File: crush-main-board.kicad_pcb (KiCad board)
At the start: 2 copper layers, 27 parts, among them J1 USB_B_Micro, J10 4x4_Header, J11 3x4_Header, J12 3x4_Header, J13 6x2_Header, J14 3x1_Header, J2 3x3 Header, J3 3x3 Header, J4 3x3 Header, J5 3x2 Header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

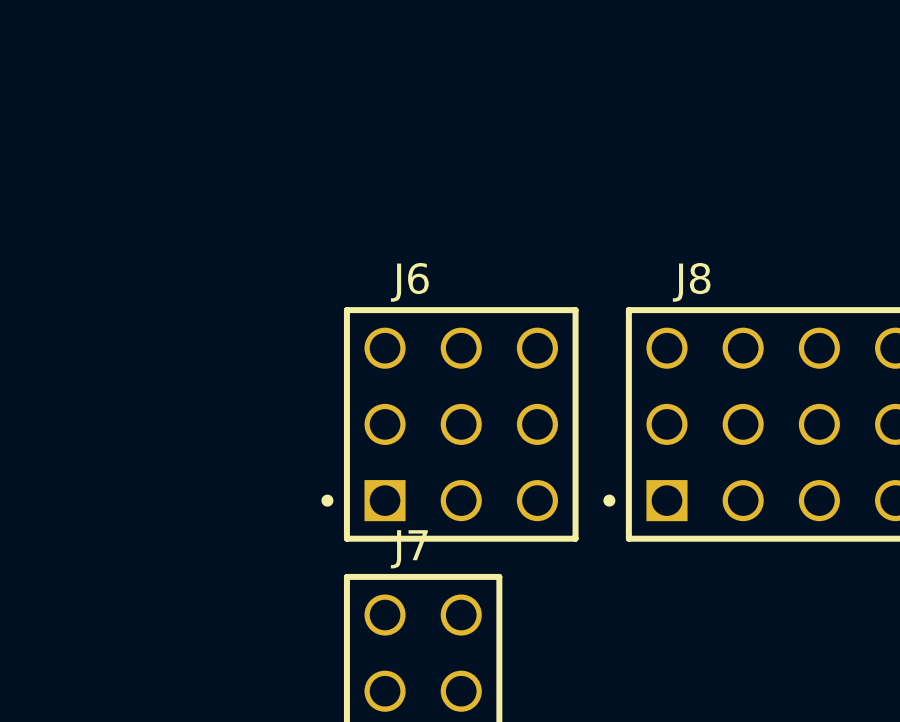
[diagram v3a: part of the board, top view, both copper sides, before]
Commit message: Fixed SPI header and updated footprint accordingly
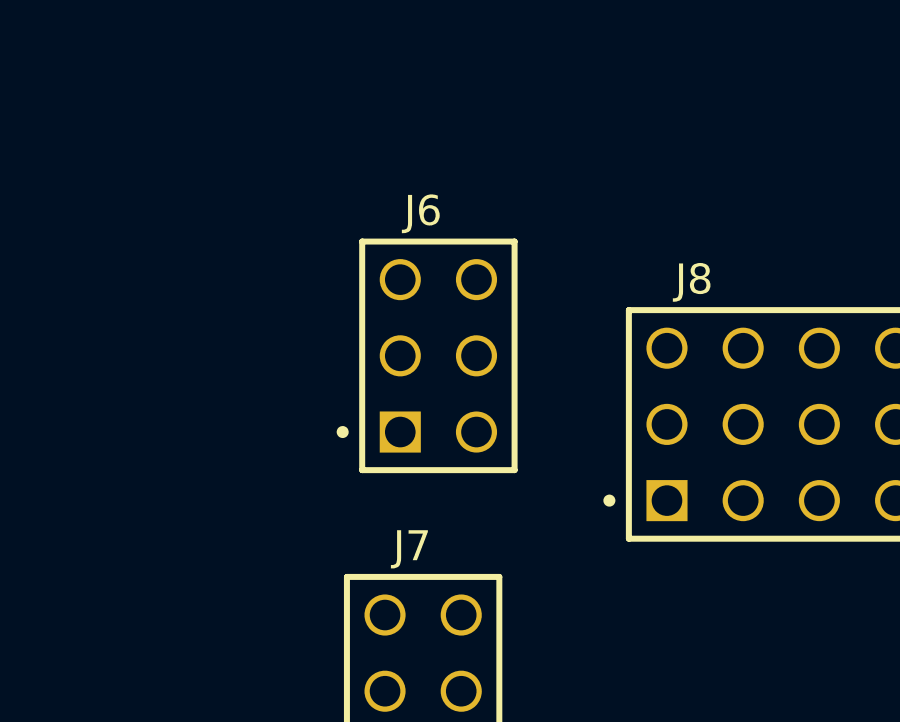
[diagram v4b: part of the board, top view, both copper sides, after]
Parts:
- J6: value 3x3 Header -> 3x2 Header; footprint Crush_Mainboard_Footprints:3x3_Header -> Crush_Mainboard_Footprints:3x2_Header
- moved J6 2.41 mm to (113.0, 104.1)
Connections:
- J13 pad 06: SPI_CS -> DIO30
- J6 pad 01: DIO30 -> DIO31
- J6 pad 04: DIO31 -> DIO32

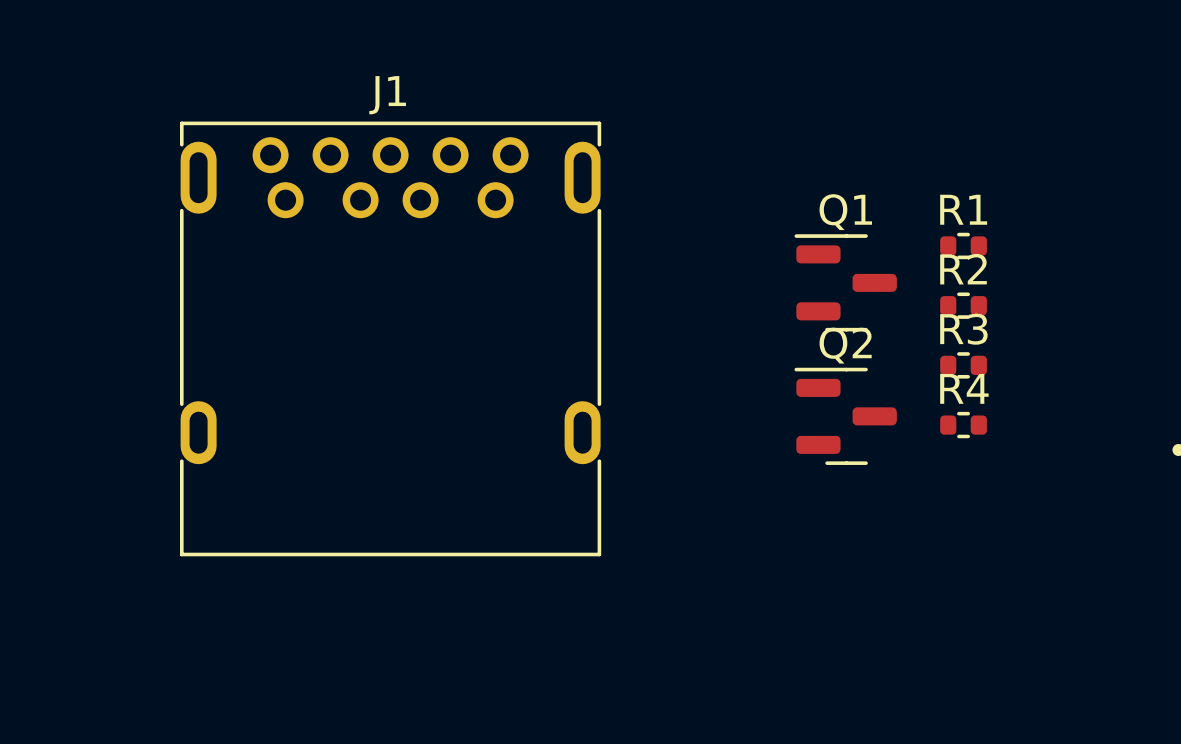
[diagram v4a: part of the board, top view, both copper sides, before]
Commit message: Added thruster battery monitoring circuit
There is no footprint assigned for an I2C isolator and resistors yet
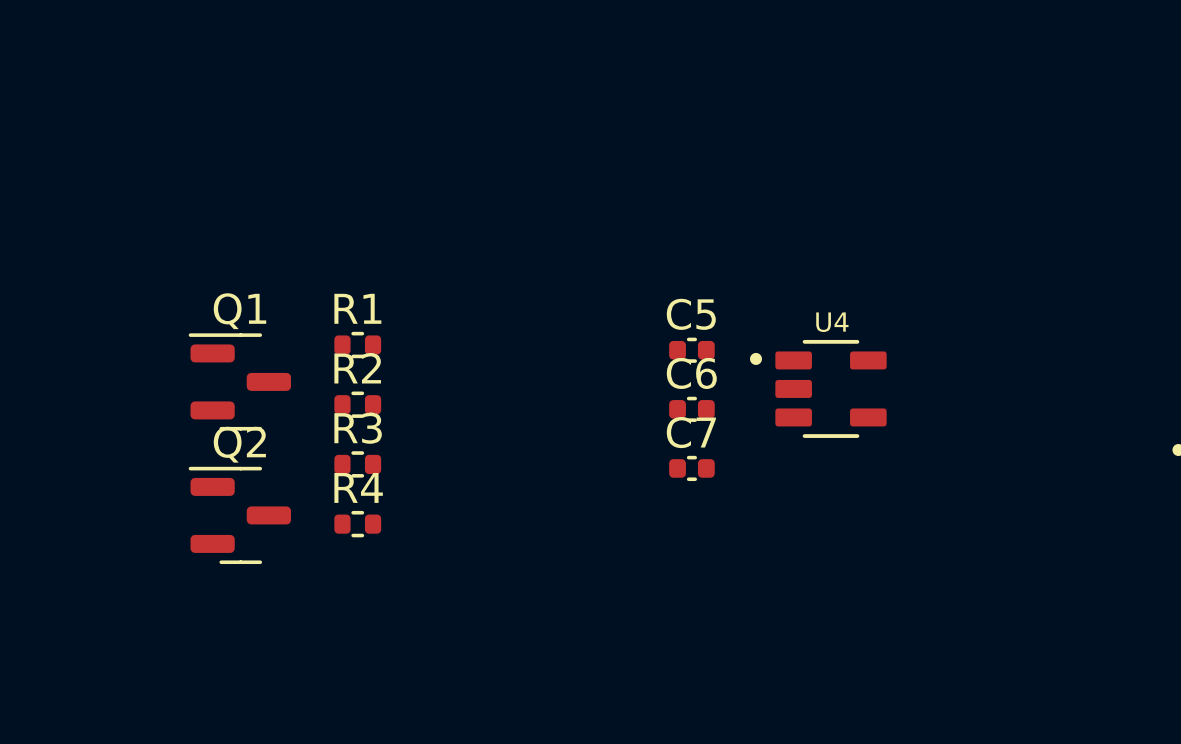
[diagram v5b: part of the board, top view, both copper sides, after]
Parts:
- removed J1: USB_B_Micro, Connector_USB:USB3_A_Molex_48393-001
- added C5: 0u1, Capacitor_SMD:C_0402_1005Metric, F.Cu at (148.9, 32.8)
- added C6: 0u1, Capacitor_SMD:C_0402_1005Metric, F.Cu at (148.9, 34.8)
- added C7: 0u1, Capacitor_SMD:C_0402_1005Metric, F.Cu at (148.9, 36.8)
- added U4: MCP3221A5T-I/OT, Crush_Mainboard_Footprints:SOT95P280X145-5N, F.Cu at (153.6, 34.1)
- C1, C2, C3, C4: value 0.1 uF -> 0u1
- moved Q1 20.5 mm to (133.9, 33.9)
- moved Q2 20.5 mm to (133.9, 38.3)
- moved R1 20.5 mm to (137.8, 32.6)
- moved R2 20.5 mm to (137.8, 34.6)
- moved R3 20.5 mm to (137.8, 36.6)
- moved R4 20.5 mm to (137.8, 38.6)
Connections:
- J13 pad 06: DIO30 -> SPI_CS
- J13 pad 12: SPI_CS -> DIO30

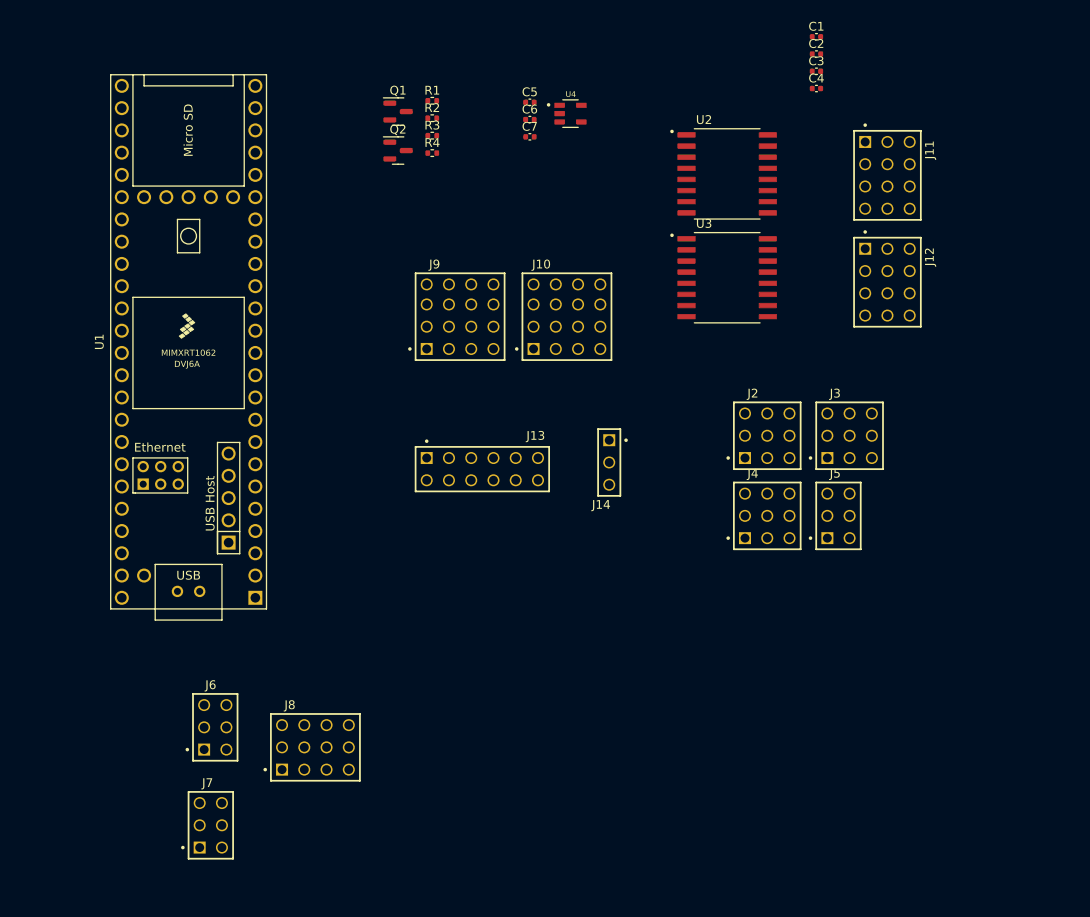
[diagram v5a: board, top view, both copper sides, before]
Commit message: Added diode and header for remaining pins, fixed signal battery monitor
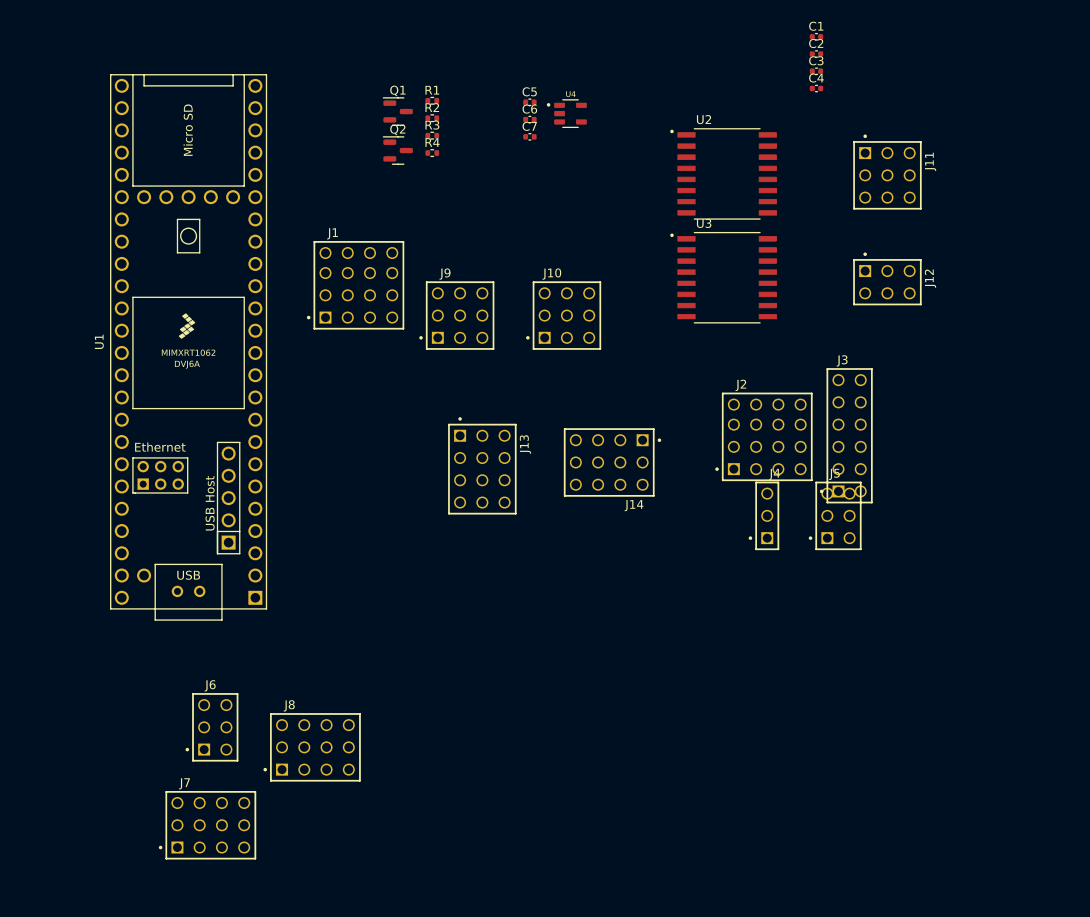
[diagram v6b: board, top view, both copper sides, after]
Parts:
- added J1: 4x4_Header, Crush_Mainboard_Footprints:4x4_Header, F.Cu at (129.4, 53.6)
- J10, J9: value 4x4_Header -> 3x3 Header; footprint Crush_Mainboard_Footprints:4x4_Header -> Crush_Mainboard_Footprints:3x3_Header
- J11: value 3x4_Header -> 3x3 Header; footprint Crush_Mainboard_Footprints:3x4_Header -> Crush_Mainboard_Footprints:3x3_Header
- J12: value 3x4_Header -> 3x2 Header; footprint Crush_Mainboard_Footprints:3x4_Header -> Crush_Mainboard_Footprints:3x2_Header
- J13: value 6x2_Header -> 3x4_Header; footprint Crush_Mainboard_Footprints:6x2_Header -> Crush_Mainboard_Footprints:3x4_Header
- J14: value 3x1_Header -> 3x4_Header; footprint Crush_Mainboard_Footprints:3x1_Header -> Crush_Mainboard_Footprints:3x4_Header
- J2: value 3x3 Header -> 4x4_Header; footprint Crush_Mainboard_Footprints:3x3_Header -> Crush_Mainboard_Footprints:4x4_Header
- J3: value 3x3 Header -> 6x2_Header; footprint Crush_Mainboard_Footprints:3x3_Header -> Crush_Mainboard_Footprints:6x2_Header
- J4: value 3x3 Header -> 3x1_Header; footprint Crush_Mainboard_Footprints:3x3_Header -> Crush_Mainboard_Footprints:3x1_Header
- J7: value 3x2 Header -> 3x4 Header; footprint Crush_Mainboard_Footprints:3x2_Header -> Crush_Mainboard_Footprints:3x4_Header
- J8: value 3x4_Header -> 3x4 Header
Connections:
- J10 pad 01: +5V -> PWM23
- J10 pad 02: SDA_5V -> +5V
- J10 pad 03: SCL_5V -> GND
- J10 pad 04: GND -> PWM24
- J10 pad 06: SDA_5V -> GND
- J10 pad 07: SCL_5V -> PWM25
- J10 pad 08: GND -> +5V
- J10 pad 09: +5V -> GND
- J11 pad 01: +3V3 -> PWM33
- J11 pad 02: PWM2_T -> +5V
- J11 pad 04: +3V3 -> PWM36
- J11 pad 05: PWM3_T -> +5V
- J11 pad 07: +3V3 -> PWM37
- J11 pad 08: PWM4_T -> +5V
- J12 pad 01: +3V3 -> PWM28
- J12 pad 02: PWM6_T -> +5V
- J12 pad 04: +3V3 -> PWM29
- J12 pad 05: PWM7_T -> +5V
- J13 pad 01: GND -> +3V3
- J13 pad 02: +3V3 -> PWM2_T
- J13 pad 03: SPI_SDI -> GND
- J13 pad 04: SPI_SCK -> +3V3
- J13 pad 05: SPI_SDO -> PWM3_T
- J13 pad 06: SPI_CS -> GND
- J13 pad 07: GND -> +3V3
- J13 pad 08: +3V3 -> PWM4_T
- J13 pad 09: SPI_SDI -> GND
- J13 pad 10: SPI_SCK -> +3V3
- J13 pad 11: SPI_SDO -> PWM5_T
- J13 pad 12: DIO30 -> GND
- J14 pad 01: UART_RX -> +3V3
- J14 pad 02: UART_TX -> PWM6_T
- J2 pad 01: PWM14 -> +5V
- J2 pad 02: +5V -> SDA_5V
- J2 pad 03: GND -> SCL_5V
- J2 pad 04: PWM15 -> GND
- J2 pad 06: GND -> SDA_5V
- J2 pad 07: PWM22 -> SCL_5V
- J2 pad 08: +5V -> GND
- J2 pad 09: GND -> +5V
- J3 pad 01: PWM33 -> GND
- J3 pad 02: +5V -> +3V3
- J3 pad 03: GND -> SPI_SDI
- J3 pad 04: PWM36 -> SPI_SCK
- J3 pad 05: +5V -> SPI_SDO
- J3 pad 06: GND -> SPI_CS
- J3 pad 07: PWM37 -> GND
- J3 pad 08: +5V -> +3V3
- J3 pad 09: GND -> SPI_SDI
- J4 pad 01: PWM23 -> UART_RX
- J4 pad 02: +5V -> UART_TX
- J5 pad 01: PWM28 -> DIO31
- J5 pad 02: +5V -> +3V3
- J5 pad 04: PWM29 -> DIO32
- J5 pad 05: +5V -> +3V3
- J6 pad 01: DIO31 -> DIO34
- J6 pad 02: +3V3 -> +5V
- J6 pad 04: DIO32 -> DIO35
- J6 pad 05: +3V3 -> +5V
- J7 pad 01: DIO34 -> A/DIO38
- J7 pad 02: +5V -> +3V3
- J7 pad 04: DIO35 -> A/DIO39
- J7 pad 05: +5V -> +3V3
- J8 pad 01: A/DIO38 -> A/DIO16
- J8 pad 04: A/DIO39 -> A/DIO17
- J8 pad 07: A/DIO40 -> A/DIO20
- J8 pad 10: A/DIO41 -> A/DIO21
- J9 pad 01: +5V -> PWM14
- J9 pad 02: SDA_3V3 -> +5V
- J9 pad 03: SCL_3V3 -> GND
- J9 pad 04: GND -> PWM15
- J9 pad 06: SDA_3V3 -> GND
- J9 pad 07: SCL_3V3 -> PWM22
- J9 pad 08: GND -> +5V
- J9 pad 09: +5V -> GND
- U1 pad 18: unconnected-(U1-26_A12_MOSI1-Pad18) -> A/DIO26
- U1 pad 48: +5V -> Net-(D1-K)
- U1 pad 55: USB_5V -> unconnected-(U1-5V-Pad55)
- U1 pad 56: USB_D- -> unconnected-(U1-D--Pad56)
- U1 pad 57: USB_D+ -> unconnected-(U1-D+-Pad57)

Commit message: Added connection to the power board; and the remaining footprints
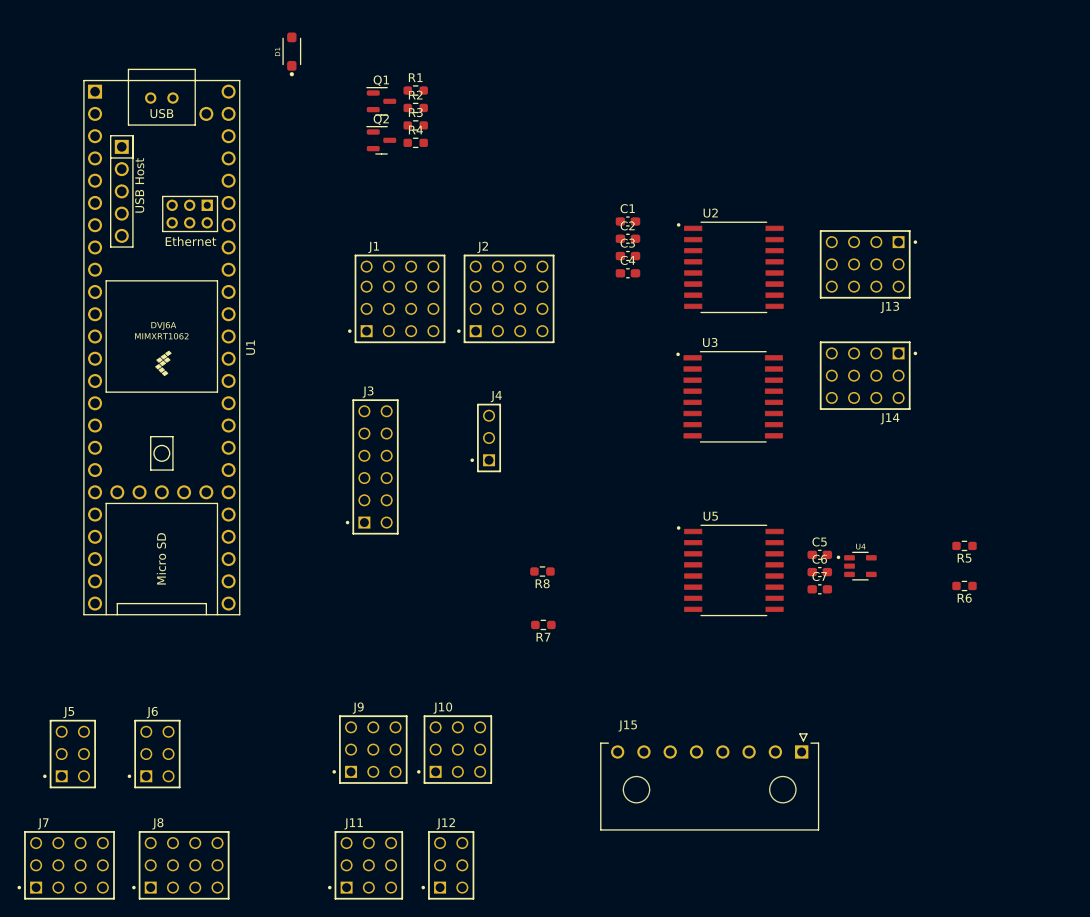
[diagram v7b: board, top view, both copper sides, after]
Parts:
- added D1: SM5817PL-TP, Crush_Mainboard_Footprints:SODFL3718X108N, F.Cu at (121.8, 27.0)
- added J15: 2157601008, Crush_Mainboard_Footprints:MOLEX_2157601008, F.Cu at (179.9, 107.0)
- added R5: 40K, Resistor_SMD:R_0603_1608Metric_Pad0.98x0.95mm_HandSolder, F.Cu at (198.5, 83.4)
- added R6: 10K, Resistor_SMD:R_0603_1608Metric_Pad0.98x0.95mm_HandSolder, F.Cu at (198.5, 88.0)
- added R7: 40K, Resistor_SMD:R_0603_1608Metric_Pad0.98x0.95mm_HandSolder, F.Cu at (150.5, 92.5)
- added R8: 10K, Resistor_SMD:R_0603_1608Metric_Pad0.98x0.95mm_HandSolder, F.Cu at (150.4, 86.4)
- added U5: ISO1640DBR, Crush_Mainboard_Footprints:SOIC127P1030X265-16N, F.Cu at (172.2, 86.2)
- C1, C2, C3, C4, C5, C6, C7: footprint Capacitor_SMD:C_0402_1005Metric -> Capacitor_SMD:C_0603_1608Metric_Pad1.08x0.95mm_HandSolder
- R1, R2, R3, R4: footprint Resistor_SMD:R_0402_1005Metric -> Resistor_SMD:R_0603_1608Metric_Pad0.98x0.95mm_HandSolder
- moved J11 98.5 mm to (130.6, 119.9), turned to 0 degrees
- moved J5 91.5 mm to (96.8, 107.2)
- moved J12 83.1 mm to (140.0, 119.9), turned to 0 degrees
- moved C5 61.3 mm to (182.0, 84.5)
- moved C6 61.3 mm to (182.0, 86.4)
- moved U4 61.3 mm to (186.7, 85.7)
- moved C7 61.3 mm to (182.0, 88.4)
- moved J3 54.2 mm to (131.3, 74.4)
- moved J10 51.1 mm to (140.7, 106.7)
- moved J9 50.5 mm to (131.1, 106.7)
- moved J13 49.5 mm to (187.2, 51.3), turned to 180 degrees
- moved J2 33.4 mm to (146.6, 55.1)
- moved J4 33.0 mm to (144.3, 71.1)
- moved J14 30.8 mm to (187.2, 64.0)
- moved C1 30.1 mm to (160.1, 46.4)
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
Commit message: Fixed an error of the "3V3_T" and "GND_T" and added some conditions for the PCB design
The power nets for the thruster side require their own custom symbols unless they will refer to the same ones that are linked to the normal power nets
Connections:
- C2 pad 1: GND -> GND_T
- C4 pad 1: GND -> GND_T
- C4 pad 2: +3V3 -> +3V3_T
- C6 pad 1: GND -> GND_T
- C7 pad 1: GND -> GND_T
- J13 pad 01: +3V3 -> +3V3_T
- J13 pad 03: GND -> GND_T
- J13 pad 04: +3V3 -> +3V3_T
- J13 pad 06: GND -> GND_T
- J13 pad 07: +3V3 -> +3V3_T
- J13 pad 09: GND -> GND_T
- J13 pad 10: +3V3 -> +3V3_T
- J13 pad 12: GND -> GND_T
- J14 pad 01: +3V3 -> +3V3_T
- J14 pad 03: GND -> GND_T
- J14 pad 04: +3V3 -> +3V3_T
- J14 pad 06: GND -> GND_T
- J14 pad 07: +3V3 -> +3V3_T
- J14 pad 09: GND -> GND_T
- J14 pad 10: +3V3 -> +3V3_T
- J14 pad 12: GND -> GND_T
- J15 pad 1: +5V -> +3V3
- J15 pad 7: +3V3 -> +3V3_T
- J15 pad 8: GND -> GND_T
- R6 pad 2: GND -> GND_T
- U2 pad 10: +3V3 -> +3V3_T
- U2 pad 15: GND -> GND_T
- U2 pad 9: GND -> GND_T
- U3 pad 10: +3V3 -> +3V3_T
- U3 pad 15: GND -> GND_T
- U3 pad 16: +3V3 -> +3V3_T
- U3 pad 9: GND -> GND_T
- U4 pad 2: GND -> GND_T
- U5 pad 9: GND -> GND_T
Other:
- copper layers 2 -> 4
